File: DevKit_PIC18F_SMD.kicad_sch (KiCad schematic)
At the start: 25 parts, among them J1 PIC_ICSP_ICD, J2 USB_B_Mini, J5 RIGHT_PORT, J6 LEFT_PORT, SW1 SW_RST, X1 16MHz

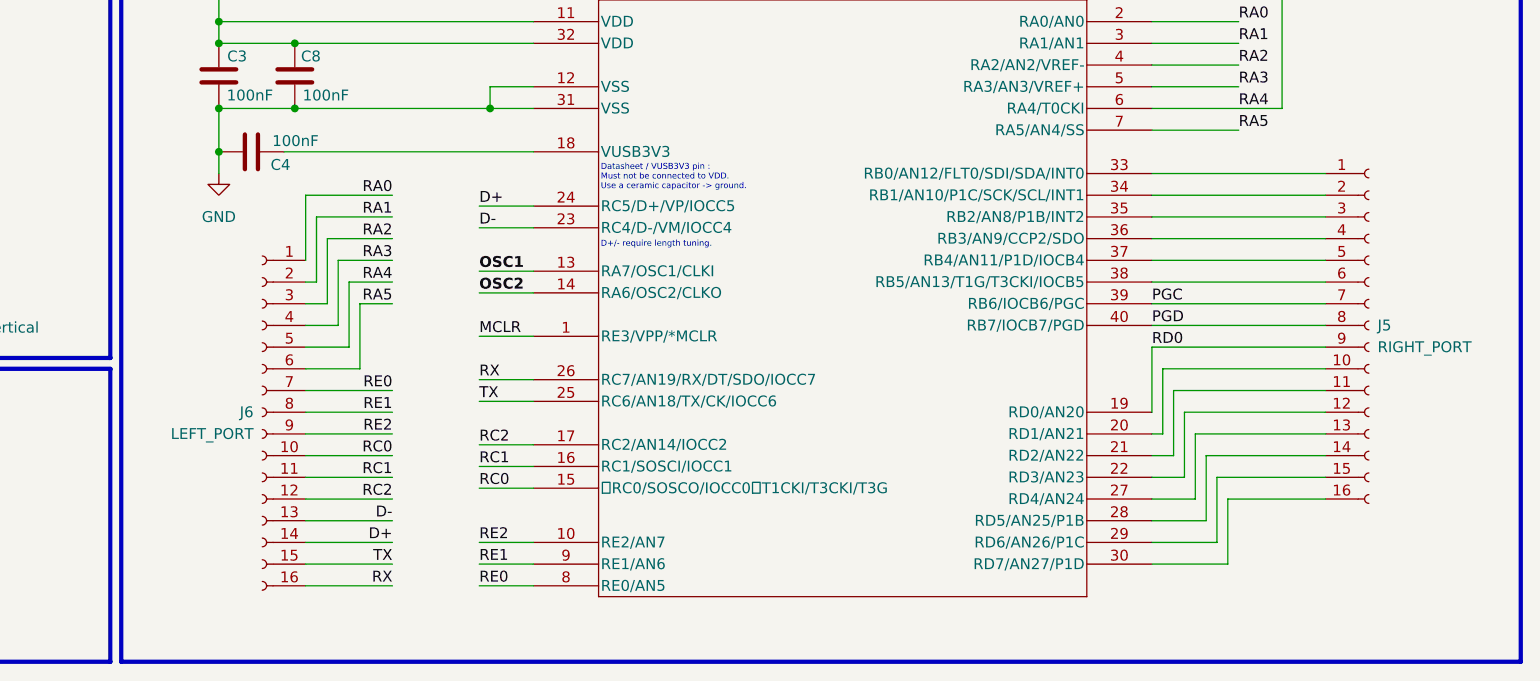
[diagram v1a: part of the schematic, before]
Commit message: Added VCC/GND pins
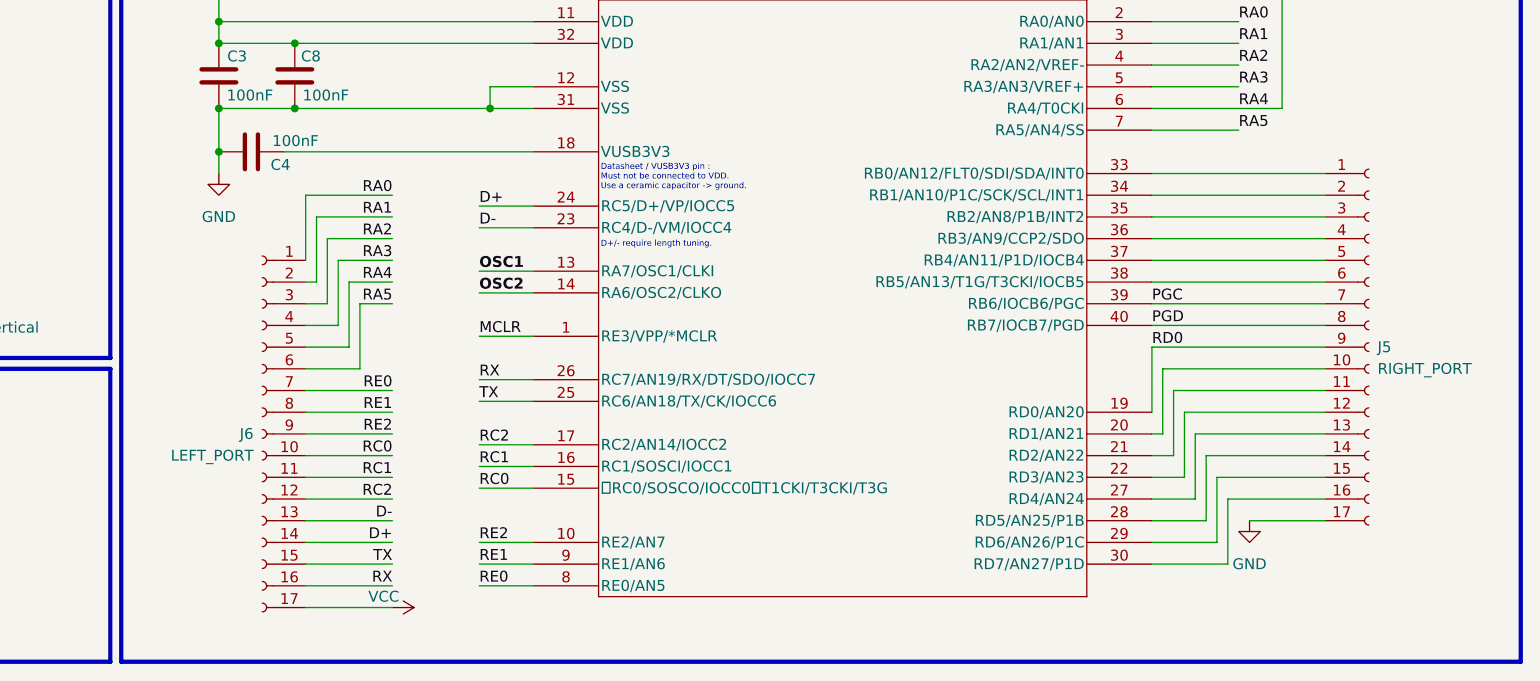
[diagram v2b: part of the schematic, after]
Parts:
- J5, J6: footprint Connector_PinHeader_2.54mm:PinHeader_1x16_P2.54mm_Vertical -> Connector_PinHeader_2.54mm:PinHeader_1x17_P2.54mm_Vertical; symbol Connector:Conn_01x16_Socket -> Connector:Conn_01x17_Socket
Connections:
- net GND: now also J5.17 (Pin_17)
- net VCC: now also J6.17 (Pin_17)
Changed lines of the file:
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@@
+	(wire
+		(pts
+			(xy 119.38 180.34) (xy 109.22 180.34)
+		)
+		(stroke
+			(width 0)
+			(type default)
+		)
+	)
 	(wire
 		(pts
@@
 		(pts
 			(xy 36.83 104.14) (xy 36.83 107.95)
+		)
+		(stroke
+			(width 0)
+			(type default)
+		)
+	)
+	(wire
+		(pts
+			(xy 219.71 170.18) (xy 228.6 170.18)
 		)
 		(stroke
@@
 	)
 	(symbol
+		(lib_id "power:VCC")
+		(at 119.38 180.34 270)
+		(unit 1)
+		(exclude_from_sim no)
+		(in_bom yes)
+		(on_board yes)
+		(dnp no)
+		(property "Reference" "#PWR017"
+			(at 115.57 180.34 0)
+			(effects
+				(font
+					(size 1.27 1.27)
+				)
+				(hide yes)
+			)
+		)
+		(property "Value" "VCC"
+			(at 118.364 179.07 90)
+			(effects
+				(font
+					(size 1.27 1.27)
+				)
+			)
+		)
+		(property "Footprint" ""
+			(at 119.38 180.34 0)
+			(effects
+				(font
+					(size 1.27 1.27)
+				)
+				(hide yes)
+			)
+		)
+		(property "Datasheet" ""
+			(at 119.38 180.34 0)
+			(effects
+				(font
+					(size 1.27 1.27)
+				)
+				(hide yes)
+			)
+		)
+		(property "Description" "Power symbol creates a global label with name \"VCC\""
+			(at 119.38 180.34 0)
+			(effects
+				(font
+					(size 1.27 1.27)
+				)
+				(hide yes)
+			)
+		)
+		(pin "1"
+		)
+		(instances
+			(project "DevKit_PIC18F_SMD"
+				(path "/495af0d8-3788-4f6a-8ee9-f4c61668daf8"
+					(reference "#PWR017")
+					(unit 1)
+				)
+			)
+		)
+	)
+	(symbol
 		(lib_id "Device:R_US")
 		(at 194.31 30.48 0)
@@
 	)
 	(symbol
+		(lib_id "power:GND")
+		(at 219.71 170.18 0)
+		(unit 1)
+		(exclude_from_sim no)
+		(in_bom yes)
+		(on_board yes)
+		(dnp no)
+		(fields_autoplaced yes)
+		(property "Reference" "#PWR011"
+			(at 219.71 176.53 0)
+			(effects
+				(font
+					(size 1.27 1.27)
+				)
+				(hide yes)
+			)
+		)
+		(property "Value" "GND"
+			(at 219.71 175.26 0)
+			(effects
+				(font
+					(size 1.27 1.27)
+				)
+			)
+		)
+		(property "Footprint" ""
+			(at 219.71 170.18 0)
+			(effects
+				(font
+					(size 1.27 1.27)
+				)
+				(hide yes)
+			)
+		)
+		(property "Datasheet" ""
+			(at 219.71 170.18 0)
+			(effects
+				(font
+					(size 1.27 1.27)
+				)
+				(hide yes)
+			)
+		)
+		(property "Description" "Power symbol creates a global label with name \"GND\" , ground"
+			(at 219.71 170.18 0)
+			(effects
+				(font
+					(size 1.27 1.27)
+				)
+				(hide yes)
+			)
+		)
+		(pin "1"
+		)
+		(instances
+			(project "DevKit_PIC18F_SMD"
+				(path "/495af0d8-3788-4f6a-8ee9-f4c61668daf8"
+					(reference "#PWR011")
+					(unit 1)
+				)
+			)
+		)
+	)
+	(symbol
 		(lib_id "power:VCC")
 		(at 194.31 24.13 0)
@@
 	)
 	(symbol
-		(lib_id "Connector:Conn_01x16_Socket")
-		(at 233.68 147.32 0)
+		(lib_id "Connector:Conn_01x17_Socket")
+		(at 233.68 149.86 0)
 		(unit 1)
 		(exclude_from_sim no)
@@
 		(dnp no)
 		(property "Reference" "J5"
-			(at 234.696 147.32 0)
+			(at 234.696 149.86 0)
 			(effects
 				(font
@@
 		)
 		(property "Value" "RIGHT_PORT"
-			(at 234.696 149.86 0)
+			(at 234.696 152.4 0)
 			(effects
 				(font
@@
 			)
 		)
-		(property "Footprint" "Connector_PinHeader_2.54mm:PinHeader_1x16_P2.54mm_Vertical"
-			(at 233.68 147.32 0)
+		(property "Footprint" "Connector_PinHeader_2.54mm:PinHeader_1x17_P2.54mm_Vertical"
+			(at 233.68 149.86 0)
 			(effects
 				(font
@@
 		)
 		(property "Datasheet" "~"
-			(at 233.68 147.32 0)
-			(effects
-				(font
-					(size 1.27 1.27)
-				)
-				(hide yes)
-			)
-		)
-		(property "Description" "Generic connector, single row, 01x16, script generated"
-			(at 233.68 147.32 0)
+			(at 233.68 149.86 0)
+			(effects
+				(font
+					(size 1.27 1.27)
+				)
+				(hide yes)
+			)
+		)
+		(property "Description" "Generic connector, single row, 01x17, script generated"
+			(at 233.68 149.86 0)
 			(effects
 				(font
@@
 		(pin "15"
 		)
+		(pin "17"
+		)
 		(instances
-			(project ""
+			(project "DevKit_PIC18F_SMD"
 				(path "/495af0d8-3788-4f6a-8ee9-f4c61668daf8"
 					(reference "J5")
@@
 	)
 	(symbol
-		(lib_id "Connector:Conn_01x16_Socket")
-		(at 104.14 157.48 0)
+		(lib_id "Connector:Conn_01x17_Socket")
+		(at 104.14 160.02 0)
 		(mirror y)
 		(unit 1)
@@
 		(dnp no)
 		(property "Reference" "J6"
-			(at 103.124 157.48 0)
+			(at 103.124 160.02 0)
 			(effects
 				(font
@@
 		)
 		(property "Value" "LEFT_PORT"
-			(at 103.124 160.02 0)
+			(at 103.124 162.56 0)
 			(effects
 				(font
@@
 			)
 		)
-		(property "Footprint" "Connector_PinHeader_2.54mm:PinHeader_1x16_P2.54mm_Vertical"
-			(at 104.14 157.48 0)
+		(property "Footprint" "Connector_PinHeader_2.54mm:PinHeader_1x17_P2.54mm_Vertical"
+			(at 104.14 160.02 0)
 			(effects
 				(font
@@
 		)
 		(property "Datasheet" "~"
-			(at 104.14 157.48 0)
-			(effects
-				(font
-					(size 1.27 1.27)
-				)
-				(hide yes)
-			)
-		)
-		(property "Description" "Generic connector, single row, 01x16, script generated"
-			(at 104.14 157.48 0)
+			(at 104.14 160.02 0)
+			(effects
+				(font
+					(size 1.27 1.27)
+				)
+				(hide yes)
+			)
+		)
+		(property "Description" "Generic connector, single row, 01x17, script generated"
+			(at 104.14 160.02 0)
 			(effects
 				(font
@@
 		(pin "15"
 		)
+		(pin "17"
+		)
 		(instances

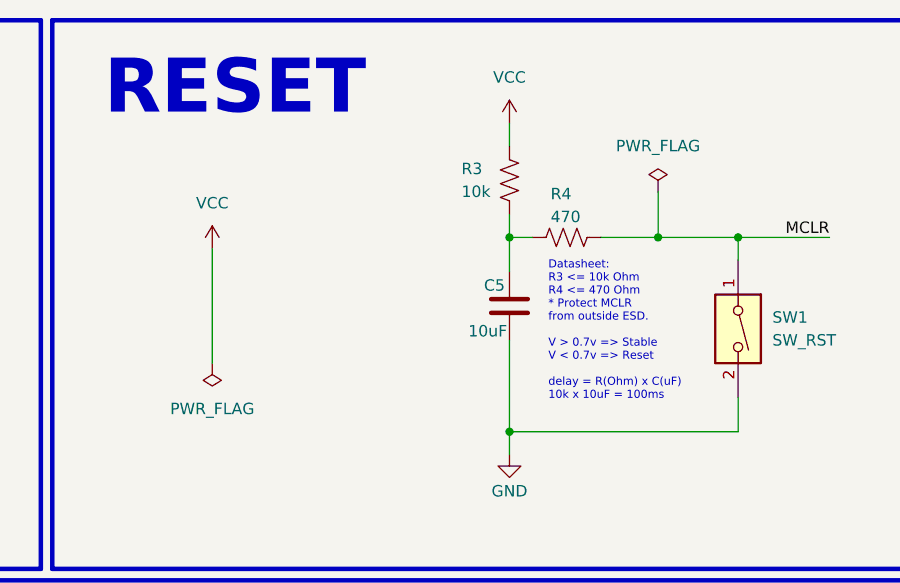
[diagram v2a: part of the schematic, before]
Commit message: Remove PWR flag in Reset part, since we updated wrong pin setup in symbol PIC18F45K50.
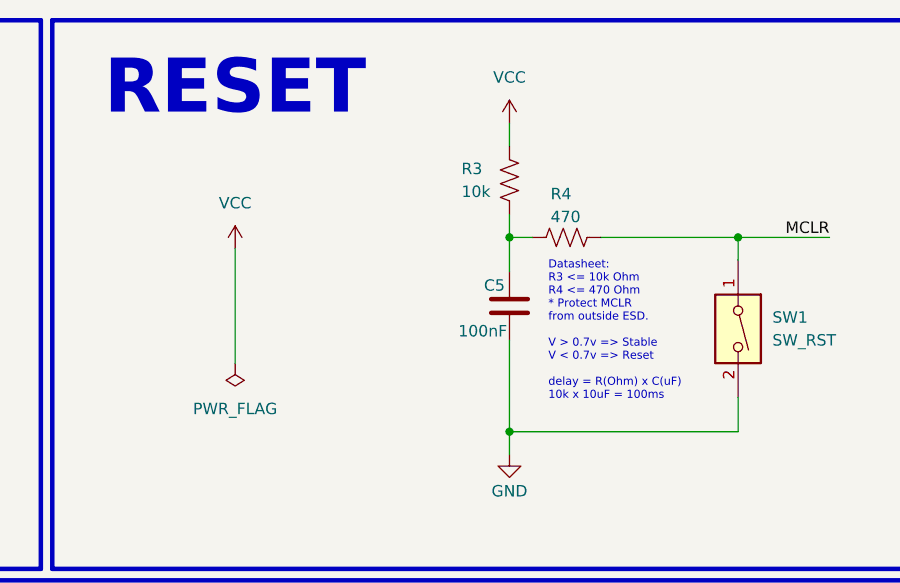
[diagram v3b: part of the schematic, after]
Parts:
- C5: value 10uF -> 100nF
- PIC18F45K50: symbol PIC18F45K50_I_P:PIC18F45K50-I_P -> PIC18F45K50_IP:PIC18F45K50-I_P
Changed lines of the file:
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@@
 					)
 				)
-				(pin power_in line
+				(pin input line
 					(at 0 -39.37 0)
 					(length 7.62)
@@
 	)
 	(junction
-		(at 210.82 36.83)
-		(diameter 0)
-		(color 0 0 0 0)
-	)
-	(junction
 		(at 194.31 58.42)
 		(diameter 0)
@@
 	(wire
 		(pts
-			(xy 210.82 36.83) (xy 219.71 36.83)
-		)
-		(stroke
-			(width 0)
-			(type default)
-		)
-	)
-	(wire
-		(pts
 			(xy 210.82 154.94) (xy 228.6 154.94)
 		)
@@
 	(wire
 		(pts
-			(xy 204.47 36.83) (xy 210.82 36.83)
+			(xy 204.47 36.83) (xy 219.71 36.83)
 		)
 		(stroke
@@
 	(wire
 		(pts
-			(xy 210.82 31.75) (xy 210.82 36.83)
-		)
-		(stroke
-			(width 0)
-			(type default)
-		)
-	)
-	(wire
-		(pts
 			(xy 129.54 156.21) (xy 135.89 156.21)
 		)
@@
 	(wire
 		(pts
-			(xy 161.29 38.1) (xy 161.29 50.8)
+			(xy 163.83 38.1) (xy 163.83 50.8)
 		)
 		(stroke
@@
 	)
 	(symbol
-		(lib_id "power:PWR_FLAG")
-		(at 210.82 31.75 0)
-		(unit 1)
-		(exclude_from_sim no)
-		(in_bom yes)
-		(on_board yes)
-		(dnp no)
-		(fields_autoplaced yes)
-		(property "Reference" "#FLG01"
-			(at 210.82 29.845 0)
-			(effects
-				(font
-					(size 1.27 1.27)
-				)
-				(hide yes)
-			)
-		)
-		(property "Value" "PWR_FLAG"
-			(at 210.82 26.67 0)
-			(effects
-				(font
-					(size 1.27 1.27)
-				)
-			)
-		)
-		(property "Footprint" ""
-			(at 210.82 31.75 0)
-			(effects
-				(font
-					(size 1.27 1.27)
-				)
-				(hide yes)
-			)
-		)
-		(property "Datasheet" "~"
-			(at 210.82 31.75 0)
-			(effects
-				(font
-					(size 1.27 1.27)
-				)
-				(hide yes)
-			)
-		)
-		(property "Description" "Special symbol for telling ERC where power comes from"
-			(at 210.82 31.75 0)
-			(effects
-				(font
-					(size 1.27 1.27)
-				)
-				(hide yes)
-			)
-		)
-		(pin "1"
-		)
-		(instances
-			(project "DevKit_PIC18F"
-				(path "/495af0d8-3788-4f6a-8ee9-f4c61668daf8"
-					(reference "#FLG01")
-					(unit 1)
-				)
-			)
-		)
-	)
-	(symbol
 		(lib_id "Device:Crystal")
 		(at 45.72 46.99 90)
@@
 	(symbol
 		(lib_id "power:VCC")
-		(at 161.29 38.1 0)
+		(at 163.83 38.1 0)
 		(mirror y)
 		(unit 1)
@@
 		(dnp no)
 		(property "Reference" "#PWR012"
-			(at 161.29 41.91 0)
+			(at 163.83 41.91 0)
 			(effects
 				(font
@@
 		)
 		(property "Value" "VCC"
-			(at 161.29 33.02 0)
+			(at 163.83 33.02 0)
 			(effects
 				(font
@@
 		)
 		(property "Footprint" ""
-			(at 161.29 38.1 0)
+			(at 163.83 38.1 0)
 			(effects
 				(font
@@
 		)
 		(property "Datasheet" ""
-			(at 161.29 38.1 0)
+			(at 163.83 38.1 0)
 			(effects
 				(font
@@
 		)
 		(property "Description" "Power symbol creates a global label with name \"VCC\""
-			(at 161.29 38.1 0)
+			(at 163.83 38.1 0)
 			(effects
 				(font
@@
 			)
 		)
-		(property "Value" "10uF"
+		(property "Value" "100nF"
 			(at 194.056 47.244 0)
 			(effects
@@
 	(symbol
 		(lib_id "power:PWR_FLAG")
-		(at 161.29 50.8 0)
+		(at 163.83 50.8 0)
 		(mirror x)
 		(unit 1)
@@
 		(dnp no)
 		(property "Reference" "#FLG02"
-			(at 161.29 52.705 0)
+			(at 163.83 52.705 0)
 			(effects
 				(font
@@
 		)
 		(property "Value" "PWR_FLAG"
-			(at 161.29 55.88 0)
+			(at 163.83 55.88 0)
 			(effects
 				(font
@@
 		)
 		(property "Footprint" ""
-			(at 161.29 50.8 0)
+			(at 163.83 50.8 0)
 			(effects
 				(font
@@
 		)
 		(property "Datasheet" "~"
-			(at 161.29 50.8 0)
+			(at 163.83 50.8 0)
 			(effects
 				(font
@@
 		)
 		(property "Description" "Special symbol for telling ERC where power comes from"
-			(at 161.29 50.8 0)
+			(at 163.83 50.8 0)
 			(effects
 				(font
@@
 	)
 	(symbol
-		(lib_id "PIC18F45K50_I_P:PIC18F45K50-I_P")
+		(lib_id "PIC18F45K50_IP:PIC18F45K50-I_P")
 		(at 135.89 109.22 0)
 		(unit 1)

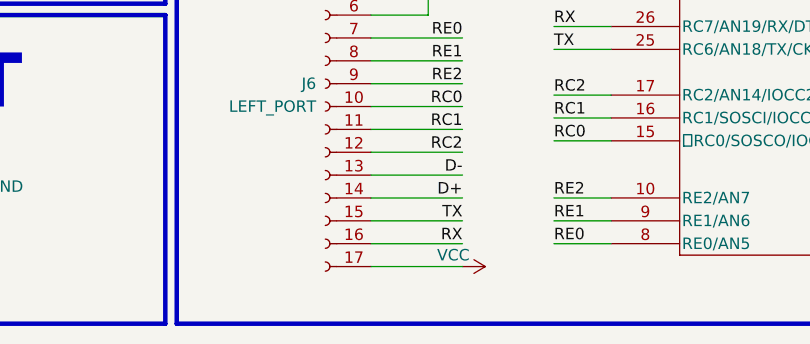
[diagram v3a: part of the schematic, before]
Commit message: rev.2 : and GND -> Left sockets & move RST_Button to bottom.
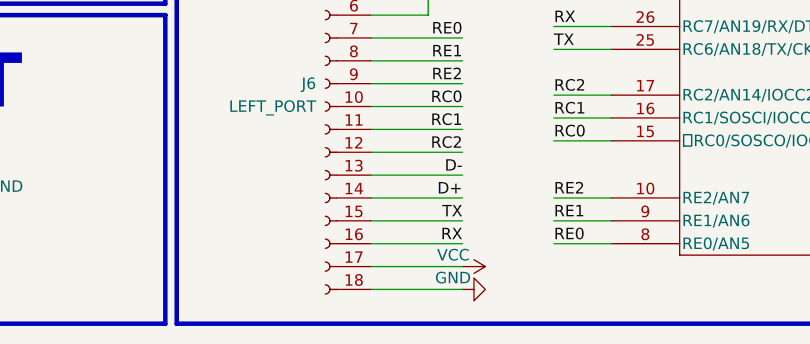
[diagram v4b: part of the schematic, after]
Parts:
- J6: footprint Connector_PinHeader_2.54mm:PinHeader_1x17_P2.54mm_Vertical -> Connector_PinHeader_2.54mm:PinHeader_1x18_P2.54mm_Vertical; symbol Connector:Conn_01x17_Socket -> Connector:Conn_01x18_Socket
- PIC18F45K50: value PIC18F45K50-I/P -> PIC18F45K50-I/MV
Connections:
- net GND: now also J6.18 (Pin_18)
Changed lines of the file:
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@@
+	(wire
+		(pts
+			(xy 109.22 182.88) (xy 119.38 182.88)
+		)
+		(stroke
+			(width 0)
+			(type default)
+		)
+	)
 	(wire
 		(pts
@@
 	)
 	(symbol
+		(lib_id "power:GND")
+		(at 119.38 182.88 90)
+		(unit 1)
+		(exclude_from_sim no)
+		(in_bom yes)
+		(on_board yes)
+		(dnp no)
+		(property "Reference" "#PWR013"
+			(at 125.73 182.88 0)
+			(effects
+				(font
+					(size 1.27 1.27)
+				)
+				(hide yes)
+			)
+		)
+		(property "Value" "GND"
+			(at 116.332 181.61 90)
+			(effects
+				(font
+					(size 1.27 1.27)
+				)
+				(justify right)
+			)
+		)
+		(property "Footprint" ""
+			(at 119.38 182.88 0)
+			(effects
+				(font
+					(size 1.27 1.27)
+				)
+				(hide yes)
+			)
+		)
+		(property "Datasheet" ""
+			(at 119.38 182.88 0)
+			(effects
+				(font
+					(size 1.27 1.27)
+				)
+				(hide yes)
+			)
+		)
+		(property "Description" "Power symbol creates a global label with name \"GND\" , ground"
+			(at 119.38 182.88 0)
+			(effects
+				(font
+					(size 1.27 1.27)
+				)
+				(hide yes)
+			)
+		)
+		(pin "1"
+		)
+		(instances
+			(project "DevKit_PIC18F_SMD"
+				(path "/495af0d8-3788-4f6a-8ee9-f4c61668daf8"
+					(reference "#PWR013")
+					(unit 1)
+				)
+			)
+		)
+	)
+	(symbol
 		(lib_id "power:VCC")
 		(at 163.83 38.1 0)
@@
 	)
 	(symbol
-		(lib_id "Connector:Conn_01x17_Socket")
+		(lib_id "Connector:Conn_01x18_Socket")
 		(at 104.14 160.02 0)
 		(mirror y)
@@
 			)
 		)
-		(property "Footprint" "Connector_PinHeader_2.54mm:PinHeader_1x17_P2.54mm_Vertical"
+		(property "Footprint" "Connector_PinHeader_2.54mm:PinHeader_1x18_P2.54mm_Vertical"
 			(at 104.14 160.02 0)
 			(effects
@@
 			)
 		)
-		(property "Description" "Generic connector, single row, 01x17, script generated"
+		(property "Description" "Generic connector, single row, 01x18, script generated"
 			(at 104.14 160.02 0)
 			(effects
@@
 		)
 		(pin "17"
+		)
+		(pin "18"
 		)
 		(instances
@@
 			)
 		)
-		(property "Description" "USB Mini Type B connector"
+		(property "Description" "USB Mini Type B connector Vertical"
 			(at 91.44 41.91 0)
 			(effects
@@
 			)
 		)
-		(property "Value" "PIC18F45K50-I/P"
+		(property "Value" "PIC18F45K50-I/MV"
 			(at 119.38 151.384 90)
 			(effects
